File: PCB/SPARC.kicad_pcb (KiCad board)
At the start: 4 copper layers, 80 x 45 mm, 91 parts, among them J1 Conn_Coaxial_Power, J2 Conn_Coaxial_Power, J3 Conn_01x06_Female, J4 Conn_01x03_Female, J5 Conn_01x03_Female, J6 Conn_01x06_Female, U1 HV2621, U2 HV2621

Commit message: Updated Gerbers
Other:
- board text added: "Original 1CH Design: Randy Palamar 2023 <palamar@ualberta.ca> 2CH Design: Kirk Rieberger March 2023 <rieberg1@ualberta.ca>"
- board text removed: "Original 1CH Design: Randy Palamar 2023 <palamar@ualberta.ca> 2CH Design: Kirk Rieberger 2023 <rieberg1@ualberta.ca>"
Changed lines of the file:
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@@
     (effects (font (size 2 2) (thickness 0.15)) (justify mirror))
   )
-  (gr_text "Original 1CH Design: Randy Palamar 2023\n<palamar@ualberta.ca>\n\n2CH Design: Kirk Rieberger 2023\n<rieberg1@ualberta.ca>" (at 123.4 57.8) (layer "B.SilkS")
+  (gr_text "Original 1CH Design: Randy Palamar 2023\n<palamar@ualberta.ca>\n\n2CH Design: Kirk Rieberger March 2023\n<rieberg1@ualberta.ca>" (at 123.4 57.8) (layer "B.SilkS")
     (effects (font (size 1.3 1.3) (thickness 0.2)) (justify mirror))
   )
@@
       (effects (font (size 1 1) (thickness 0.15)))
     )
+    (format (units 3) (units_format 1) (precision 4))
+    (style (thickness 0.15) (arrow_length 1.27) (text_position_mode 0) (extension_height 0.58642) (extension_offset 0.5) keep_text_aligned)
+  )
+  (dimension (type aligned) (layer "Dwgs.User")
+    (pts (xy 162.91 89.63) (xy 162.92 44.62))
+    (height 8.730206)
+    (gr_text "45.0100 mm" (at 170.495206 67.126685 89.98727043) (layer "Dwgs.User")
+      (effects (font (size 1 1) (thickness 0.15)))
+    )

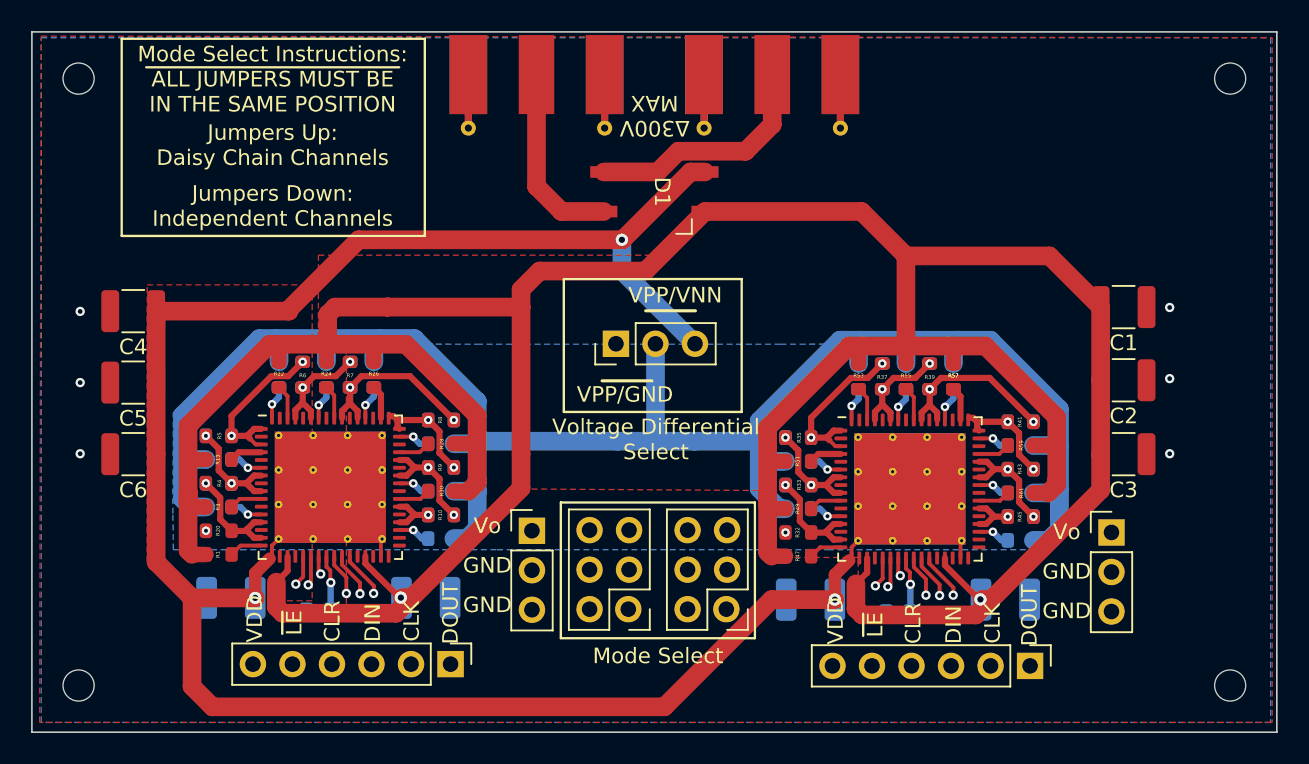
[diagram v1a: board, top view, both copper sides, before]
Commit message: Modified design rules
Fixed tracks based on PCBWay fab capabilities
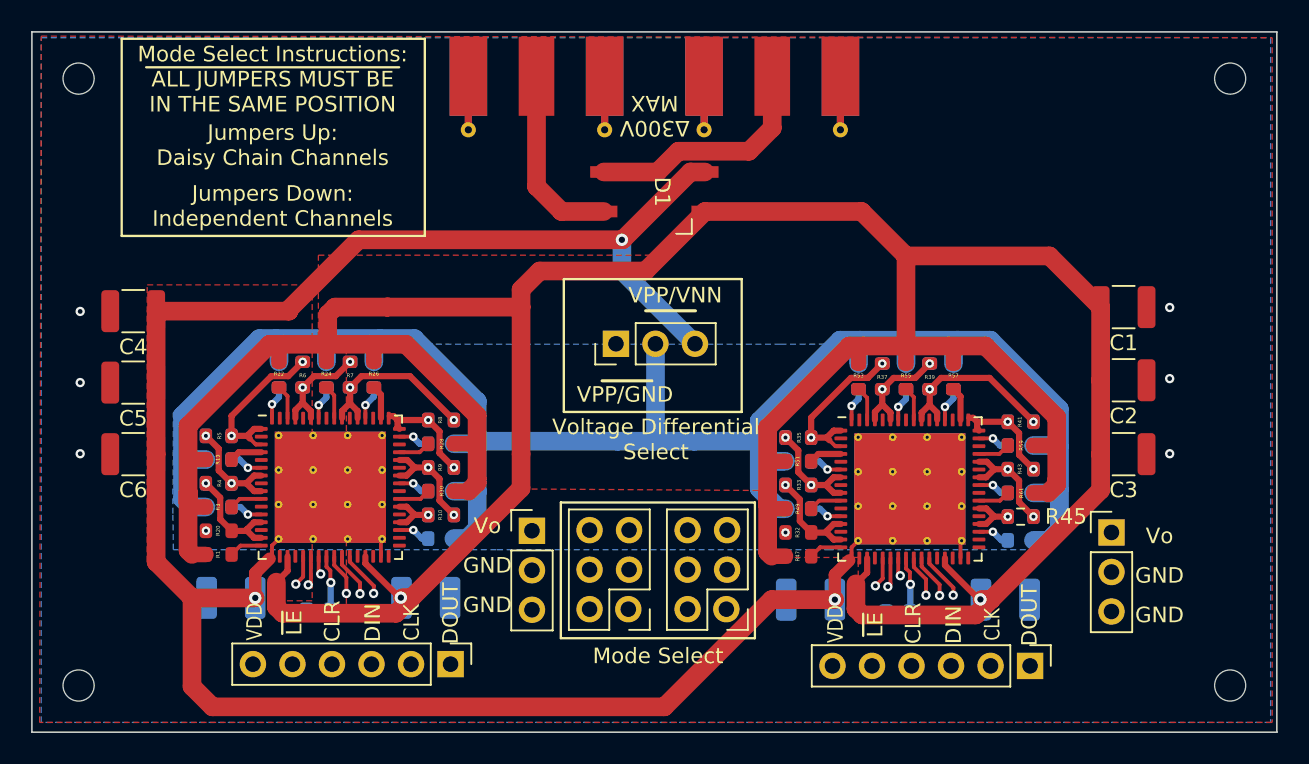
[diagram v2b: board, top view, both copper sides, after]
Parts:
- removed the R57 at (142.6, 66.8)
- R45, R46, R62: footprint grad_kicad_foot:R_0603_1608Metric_small_silk -> Resistor_SMD:R_0603_1608Metric
- moved J1 0.11 mm to (115.8, 49.2)
- moved J2 0.11 mm to (131.0, 49.2)
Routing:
- net /SRclk_1: track 30.7 -> 31.7 mm

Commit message: Changed silkscreen
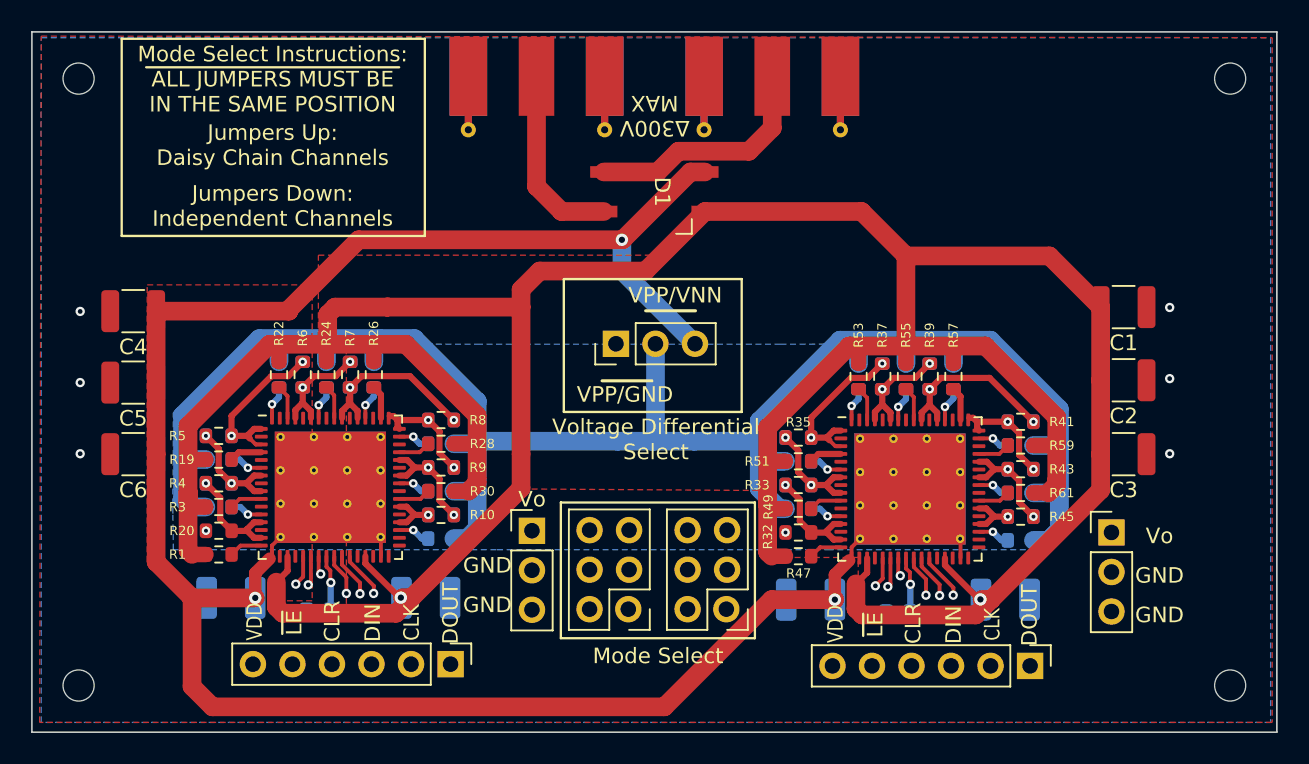
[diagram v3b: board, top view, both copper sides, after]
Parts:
- R1, R10, R11, R12, R13, R14, R15, R16, R17, R18, R19, R2, R20, R21, R22, R23, R24, R25, R26, R27, R28, R29, R3, R30, R31, R32, R33, R34, R35, R36, R37, R38, R39, R4, R40, R41, R42, R43, R44, R47, R48, R49, R5, R50, R51, R52, R53, R54, R55, R56, R57, R58, R59, R6, R60, R61, R7, R8, R9: footprint grad_kicad_foot:R_0603_1608Metric_small_silk -> grad_kicad_foot:R_0603_1608Metric_LargeSilk
- R45, R46, R62: footprint Resistor_SMD:R_0603_1608Metric -> grad_kicad_foot:R_0603_1608Metric_LargeSilk
- U1, U2: footprint Package_DFN_QFN:VQFN-64-1EP_9x9mm_P0.5mm_EP7.15x7.15mm_ThermalVias -> grad_kicad_foot:VQFN-64-1EP_9x9mm_P0.5mm_EP7.15x7.15mm_ThermalVias_0.25mm
